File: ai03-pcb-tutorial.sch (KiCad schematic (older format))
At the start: 5 parts

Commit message: set reset switch, crystal
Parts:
- added C? (x3): 0.1uF, symbol Device:C_Small
- added C?: 10uF, symbol Device:C_Small
- added C? (x2): 22pF, symbol Device:C_Small
- added R?: 10k, symbol Device:R_Small
- added SW?: SW_PUSH, symbol kbd:SW_PUSH
- added Y?: 16MHz, symbol Device:Crystal_GND24_Small
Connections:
- net labels added: D+, D-
- wire segments 20 -> 46
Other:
- moved on the sheet: C?, R?, U?

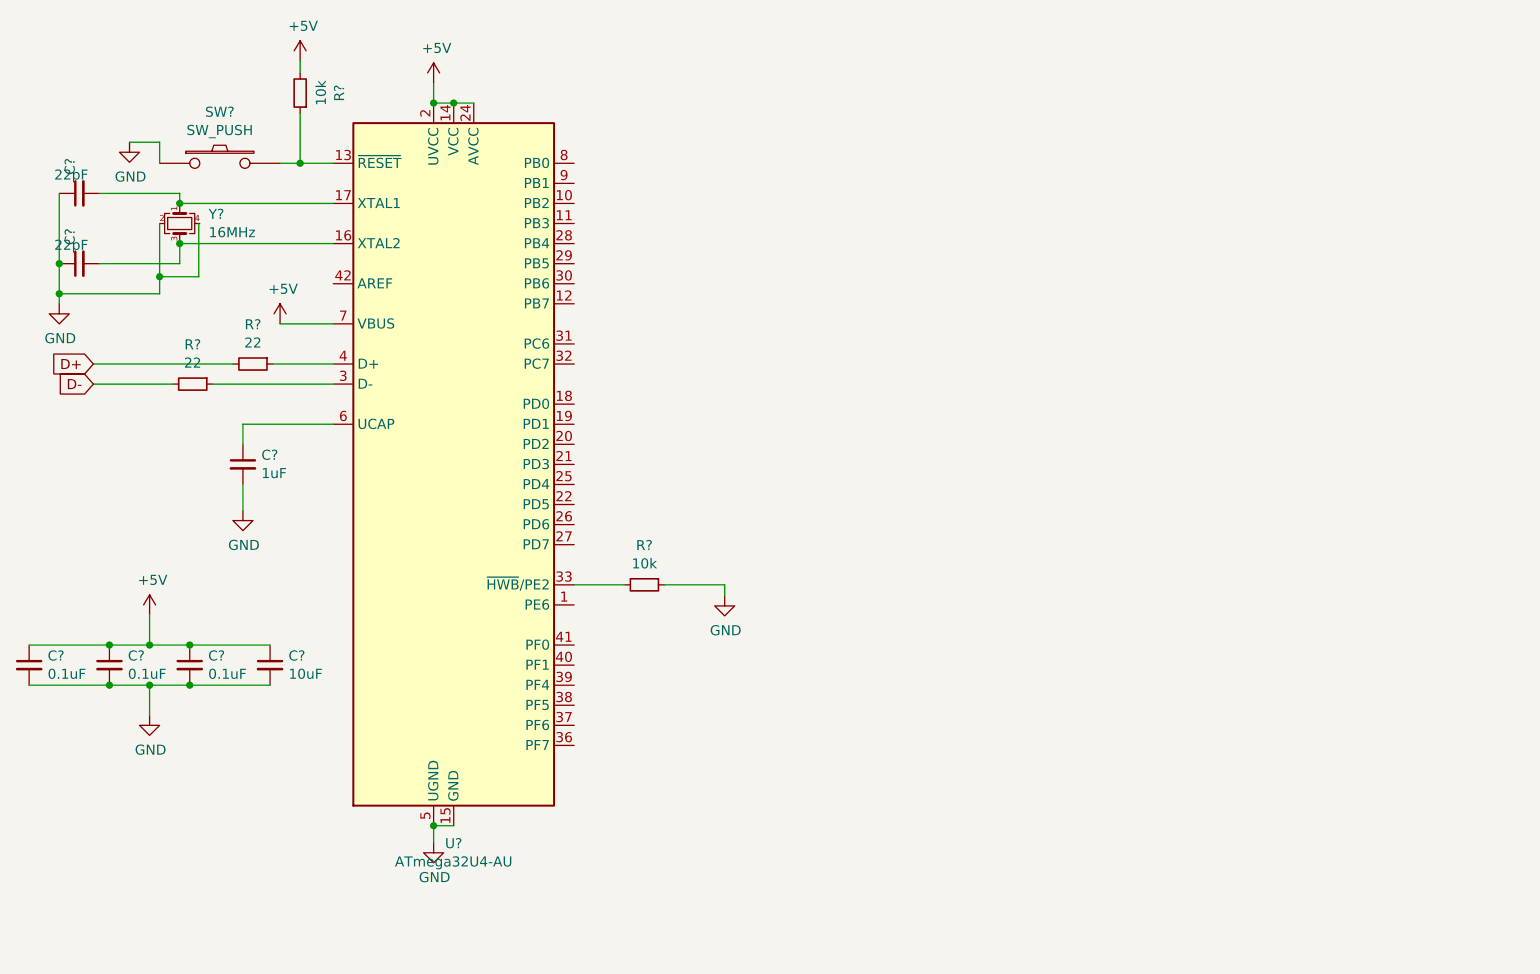
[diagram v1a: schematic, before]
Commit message: set Footprints
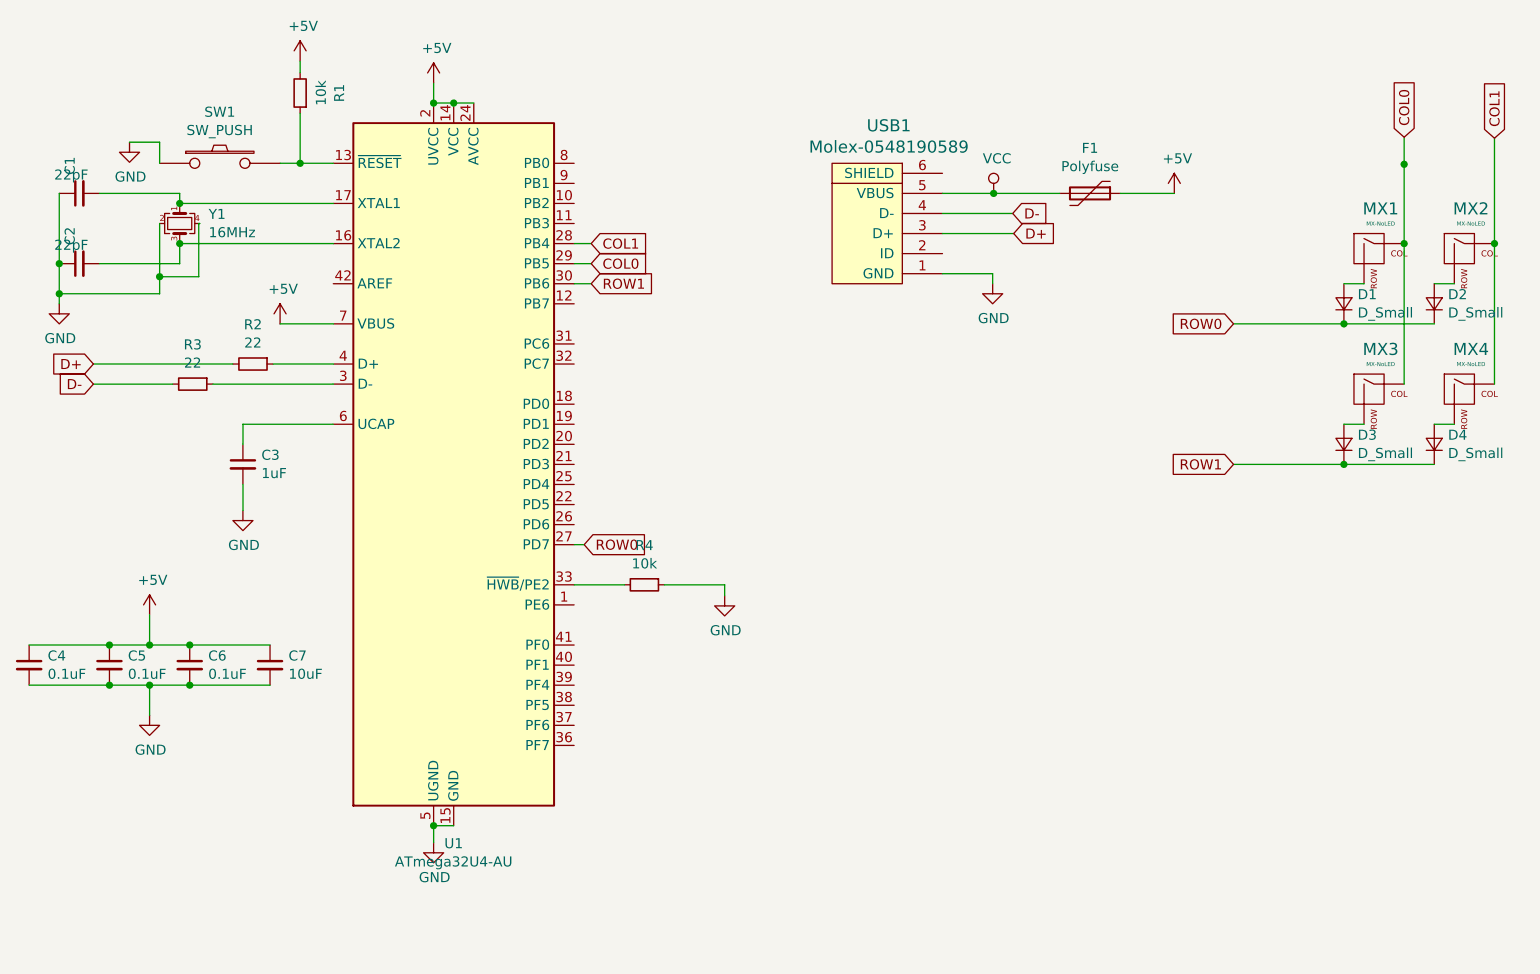
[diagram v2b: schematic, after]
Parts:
- added D1, D2, D3, D4: D_Small, Diode_SMD:D_SOD-123, symbol Device:D_Small
- added F1: Polyfuse, Fuse:Fuse_1206_3216Metric_Pad1.42x1.75mm_HandSolder, symbol Device:Polyfuse
- added MX1, MX2, MX3, MX4: MX-NoLED, MX_Alps_Hybrid:MX-1U-NoLED, symbol MX_Alps_Hybrid:MX-NoLED
- added USB1: Molex-0548190589, random-keyboard-parts:Molex-0548190589, symbol random-keyboard-parts:Molex-0548190589
- C1, C2, C3, C4, C5, C6, C7: renamed from C?; footprint (none) -> Capacitor_SMD:C_0805_2012Metric_Pad1.15x1.40mm_HandSolder
- R1, R2, R3, R4: renamed from R?; footprint (none) -> Resistor_SMD:R_0815_2038Metric_Pad1.53x4.00mm_HandSolder
- SW1: renamed from SW?; footprint (none) -> random-keyboard-parts:SKQG-1155865
- Y1: renamed from Y?; footprint (none) -> Crystal:Crystal_SMD_3225-4Pin_3.2x2.5mm_HandSoldering
- gave numbers to parts that had none: 1
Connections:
- net +5V: now also F1.1
- net D+: now also USB1.3 (D+)
- net D-: now also USB1.4 (D-)
- net GND: now also Y1.4, USB1.1 (GND)
- net ROW0: now reaches U1.27 (PD7)
- net ROW0: now also D1.1 (K), D2.1 (K)
- net COL1: now reaches U1.28 (PB4)
- net COL1: now also MX2.1 (COL), MX4.1 (COL)
- net COL0: now reaches U1.29 (PB5)
- net COL0: now also MX1.1 (COL), MX3.1 (COL)
- net ROW1: now reaches U1.30 (PB6)
- net ROW1: now also D3.1 (K), D4.1 (K)
- new net: D1.2 (A), MX1.2 (ROW)
- new net: D2.2 (A), MX2.2 (ROW)
- new net: D3.2 (A), MX3.2 (ROW)
- new net: D4.2 (A), MX4.2 (ROW)
- new net VCC: F1.2, USB1.5 (VBUS)

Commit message: chenge footprint R
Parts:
- R1, R2, R3, R4: footprint Resistor_SMD:R_0815_2038Metric_Pad1.53x4.00mm_HandSolder -> Keebio-Parts:R_0805
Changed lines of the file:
@@
 F 0 "R4" V 3869 3950 50  0000 C CNN
 F 1 "10k" V 3960 3950 50  0000 C CNN
-F 2 "Resistor_SMD:R_0815_2038Metric_Pad1.53x4.00mm_HandSolder" H 4065 3950 50  0001 C CNN
+F 2 "Keebio-Parts:R_0805" H 4065 3950 50  0001 C CNN
 F 3 "~" H 4065 3950 50  0001 C CNN
 	1    4065 3950
@@
 F 0 "R2" V 1919 2850 50  0000 C CNN
 F 1 "22" V 2010 2850 50  0000 C CNN
-F 2 "Resistor_SMD:R_0815_2038Metric_Pad1.53x4.00mm_HandSolder" H 2115 2850 50  0001 C CNN
+F 2 "Keebio-Parts:R_0805" H 2115 2850 50  0001 C CNN
 F 3 "~" H 2115 2850 50  0001 C CNN
 	1    2115 2850
@@
 F 0 "R3" V 1619 2950 50  0000 C CNN
 F 1 "22" V 1710 2950 50  0000 C CNN
-F 2 "Resistor_SMD:R_0815_2038Metric_Pad1.53x4.00mm_HandSolder" H 1815 2950 50  0001 C CNN
+F 2 "Keebio-Parts:R_0805" H 1815 2950 50  0001 C CNN
 F 3 "~" H 1815 2950 50  0001 C CNN
 	1    1815 2950
@@
 F 0 "R1" V 2154 1500 50  0000 C CNN
 F 1 "10k" V 2245 1500 50  0000 C CNN
-F 2 "Resistor_SMD:R_0815_2038Metric_Pad1.53x4.00mm_HandSolder" H 2350 1500 50  0001 C CNN
+F 2 "Keebio-Parts:R_0805" H 2350 1500 50  0001 C CNN
 F 3 "~" H 2350 1500 50  0001 C CNN
 	1    2350 1500

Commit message: adjust routeing
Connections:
- net COL1: now also U1.30 (PB6); no longer U1.28 (PB4)
- net ROW1: now also U1.28 (PB4); no longer U1.30 (PB6)
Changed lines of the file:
@@
 Wire Wire Line
 	5550 2100 5900 2100
-Text GLabel 3800 2350 2    50   Input ~ 0
-COL0
 Text GLabel 3765 3750 2    50   Input ~ 0
 ROW0
-Text GLabel 3800 2450 2    50   Input ~ 0
-ROW1
-Text GLabel 3800 2250 2    50   Input ~ 0
-COL1
-Wire Wire Line
-	3715 2250 3800 2250
-Wire Wire Line
-	3800 2350 3715 2350
 Wire Wire Line
 	3715 2450 3800 2450
@@
 	5550 2000 5805 2000
 Connection ~ 5805 2000
+Wire Wire Line
+	3795 2250 3715 2250
+Wire Wire Line
+	3800 2350 3715 2350
+Text GLabel 3800 2350 2    50   Input ~ 0
+COL0
+Text GLabel 3800 2450 2    50   Input ~ 0
+COL1
+Text GLabel 3795 2250 2    50   Input ~ 0
+ROW1
 $EndSCHEMATC
